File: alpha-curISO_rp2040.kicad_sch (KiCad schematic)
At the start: 21 parts, among them J2 SWD, U1 RP2040

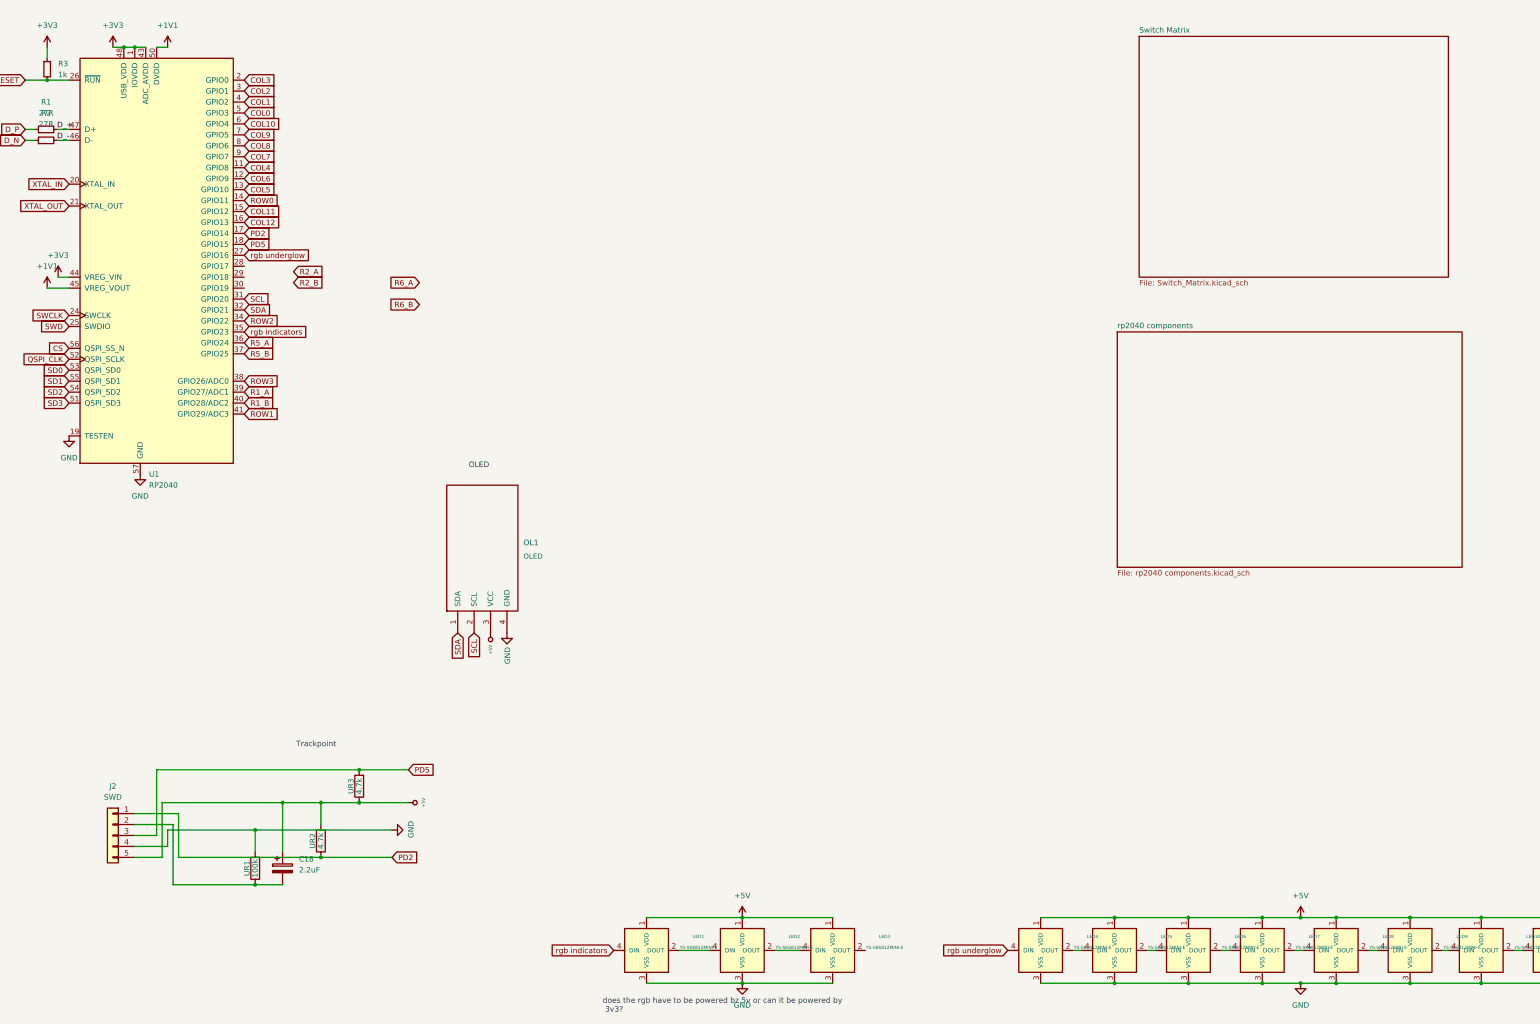
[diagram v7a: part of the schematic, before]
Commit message: first full routing
no error check, not very clean routing
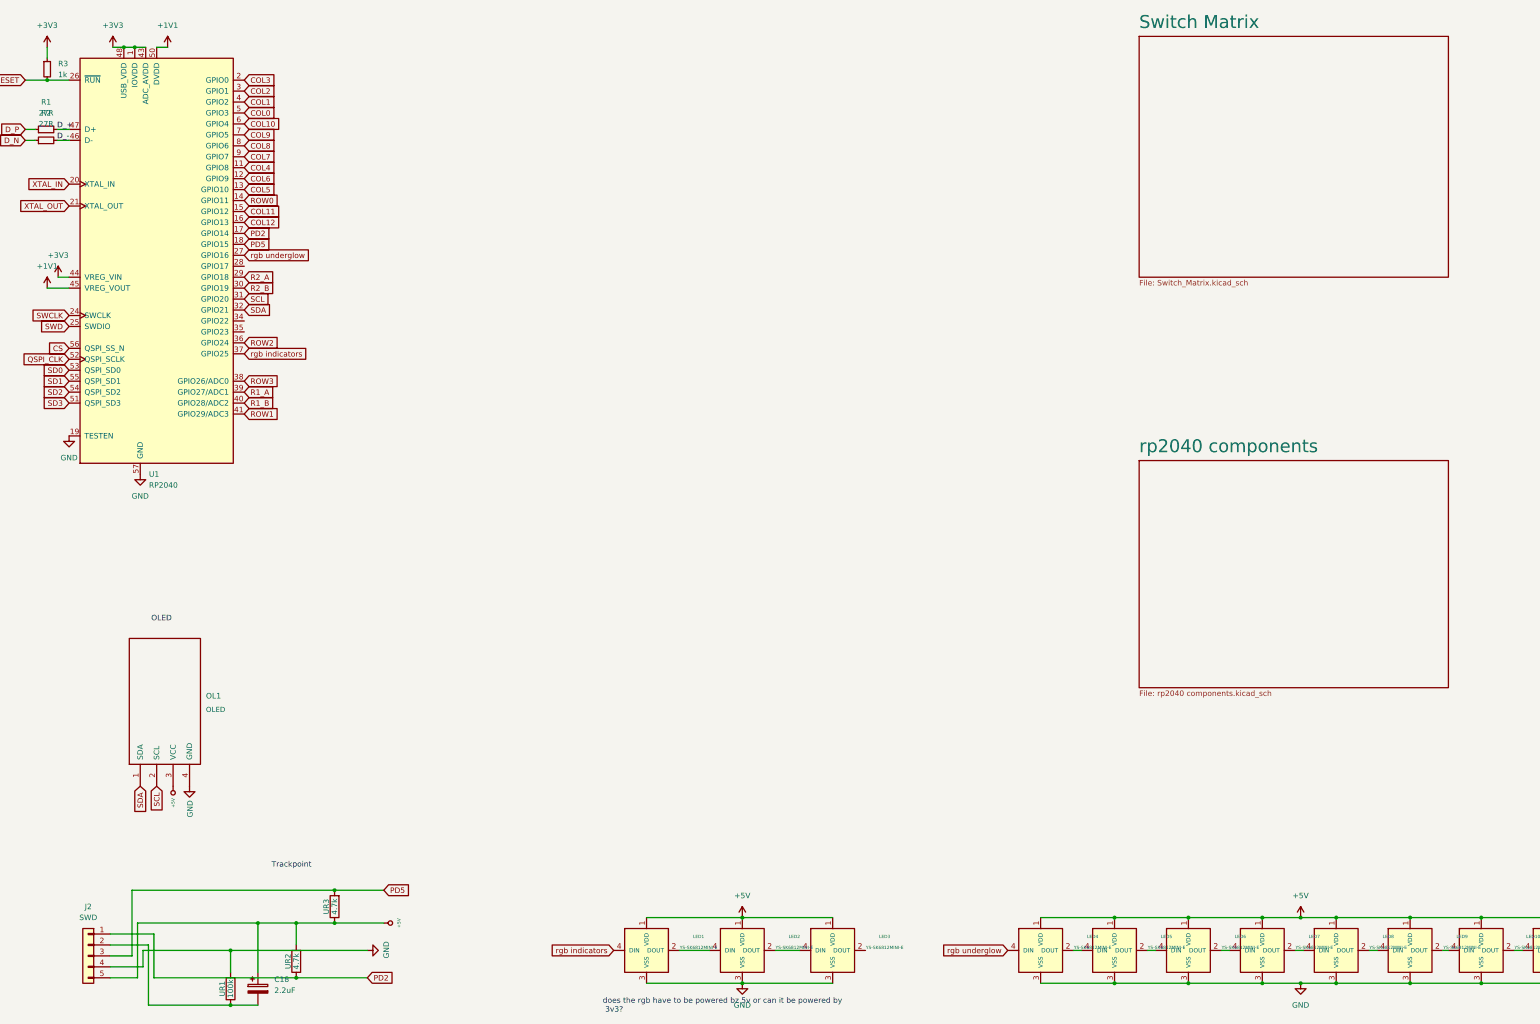
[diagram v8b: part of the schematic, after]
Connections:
- net R5_A is gone; now on net ROW2: U1.36 (GPIO24)
- net R5_B is gone; now on net rgb indicators: U1.37 (GPIO25)
- net R2_A: now also U1.29 (GPIO18)
- net R2_B: now also U1.30 (GPIO19)
- net ROW2: no longer U1.34 (GPIO22)
- net rgb indicators: no longer U1.35 (GPIO23)
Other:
- moved on the sheet: C18, J2, OL1, UR1, UR2, UR3
